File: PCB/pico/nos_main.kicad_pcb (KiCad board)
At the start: 2 copper layers, 362 x 64 mm, 159 parts, among them U1 PiPico_No_SWD, U2 ADG732BSUZ, U3 DC/DC

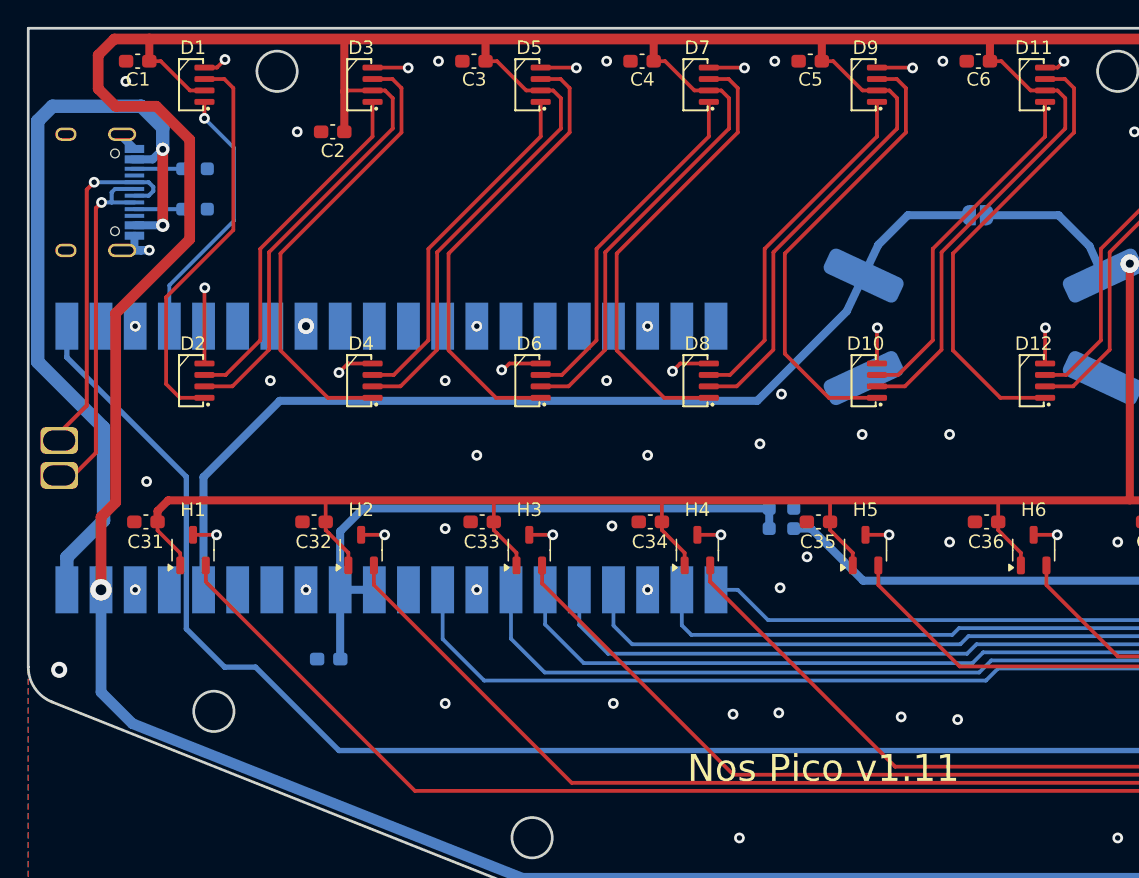
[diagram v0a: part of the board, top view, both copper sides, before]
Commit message: Nos Pico PCB v1.12 (isolate vbus)
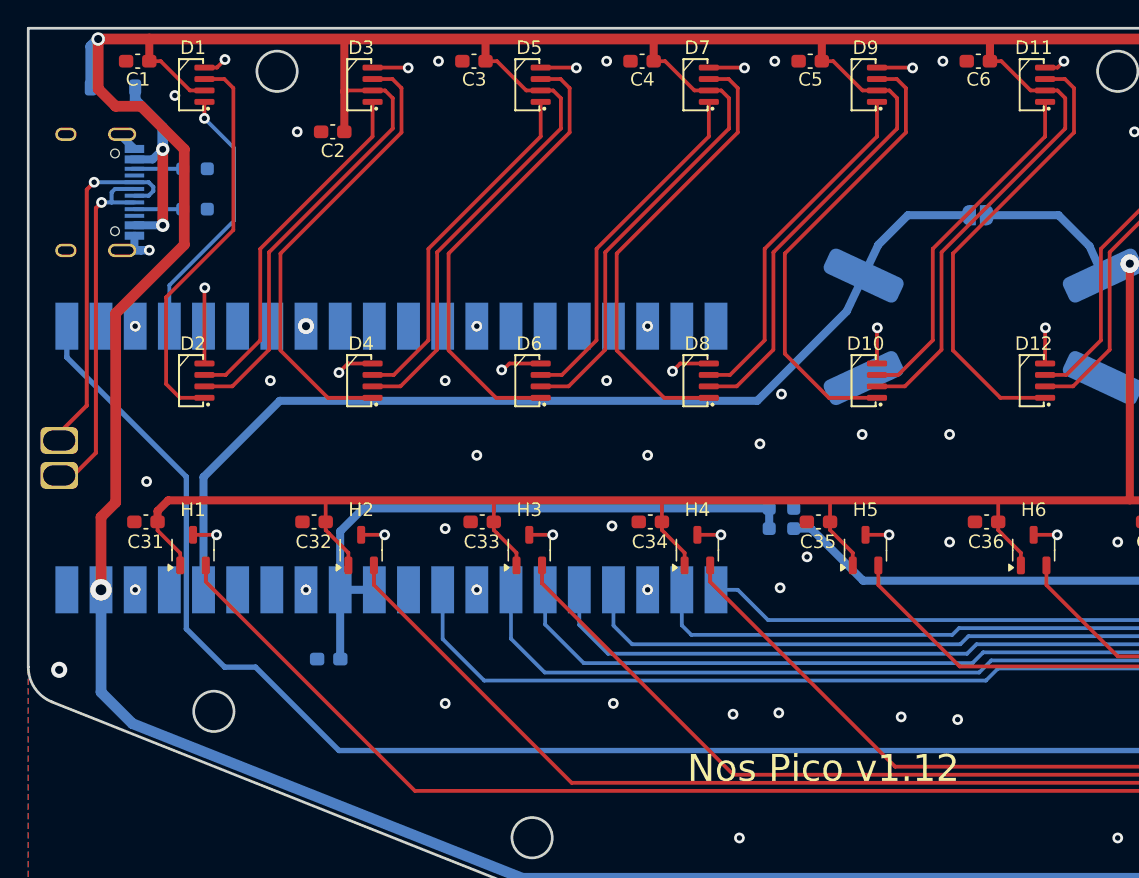
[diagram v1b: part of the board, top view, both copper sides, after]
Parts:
- added D63: MBR120VLSF, Diode_SMD:D_SOD-123, B.Cu at (38.8, 125.8)
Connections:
- U1 pad 40: VBUS -> unconnected-(U1-VBUS-Pad40)
- USB1 pad 11: VBUS -> Net-(D63-A)
- USB1 pad 2: VBUS -> Net-(D63-A)
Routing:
- net VBUS: track 60.4 -> 0.00 mm, vias 2 -> 0
- net Net-(D63-A): track 0.00 -> 15.8 mm, vias 0 -> 2
- net +5V: track 1702.5 -> 1706.1 mm, vias 7 -> 8
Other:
- board text added: "Nos Pico v1.12"
- board text removed: "Nos Pico v1.11"

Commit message: PCB project update
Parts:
- added SW1: SW_SPST, nos_main:SW_SKHHANA010_Combo, F.Cu at (94.5, 177.6)
- added SW2: SW_SPST, nos_main:SW_SKHHANA010_Combo, F.Cu at (107.5, 177.6)
- added SW3: SW_SPST, nos_main:SW_SKHHANA010_Combo, F.Cu at (319.5, 177.6)
- added SW4: SW_SPST, nos_main:SW_SKHHANA010_Combo, F.Cu at (332.5, 177.6)
- moved JP1 10.2 mm to (113.3, 135.3)
- moved R1 10.0 mm to (98.5, 158.6)
- moved R2 10.0 mm to (98.5, 157.1)
- moved U3 10.0 mm to (113.5, 143.6)
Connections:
- U1 pad 14: unconnected-(U1-GPIO10-Pad14) -> Net-(SW4-B)
- U1 pad 15: unconnected-(U1-GPIO11-Pad15) -> Net-(SW3-B)
- U1 pad 16: unconnected-(U1-GPIO12-Pad16) -> Net-(SW2-B)
- U1 pad 17: unconnected-(U1-GPIO13-Pad17) -> Net-(SW1-B)
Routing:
- net Net-(SW4-B): track 0.00 -> 313.2 mm
- net Net-(SW3-B): track 0.00 -> 310.1 mm
- net Net-(SW2-B): track 0.00 -> 133.7 mm, vias 0 -> 1
- net Net-(SW1-B): track 0.00 -> 124.8 mm, vias 0 -> 1
- net Vref: track 559.0 -> 576.8 mm
- net Net-(U1-GPIO26_ADC0): track 46.1 -> 56.1 mm
- net Net-(U2-D): track 135.2 -> 125.2 mm
- net Net-(D57-In): track 173.8 -> 183.1 mm
- net +3V3: track 74.4 -> 83.1 mm
- net GND: track 206.9 -> 200.6 mm, vias 201 -> 236
- net Net-(D15-Out): track 34.0 -> 31.1 mm
- net Net-(D13-Out): track 31.3 -> 33.7 mm
- net +5V: track 1706.1 -> 1706.7 mm
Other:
- board text added: "Nos Pico v1.2"
- board text removed: "Nos Pico v1.12"

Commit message: Nos Pico PCB v1.2 (add buttons)
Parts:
- D63: footprint Diode_SMD:D_SOD-123 -> nos_main:D_SOD-123_LONG
- H1, H10, H11, H12, H13, H14, H15, H16, H17, H18, H19, H2, H20, H21, H22, H23, H24, H25, H26, H27, H28, H3, H4, H5, H6, H7, H8, H9: footprint Package_TO_SOT_SMD:SOT-23-3 -> nos_main:SOT-23-FAT
- moved SW3 13.0 mm to (332.5, 177.6)
- moved SW4 13.0 mm to (319.5, 177.6)
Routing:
- net Net-(SW4-B): track 313.2 -> 329.3 mm
- net GND: vias 236 -> 235
